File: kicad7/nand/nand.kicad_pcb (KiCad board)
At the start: 2 copper layers, 43.2 x 27.9 mm, 15 parts, among them J1 Conn_01x06_Pin, U1 TL074

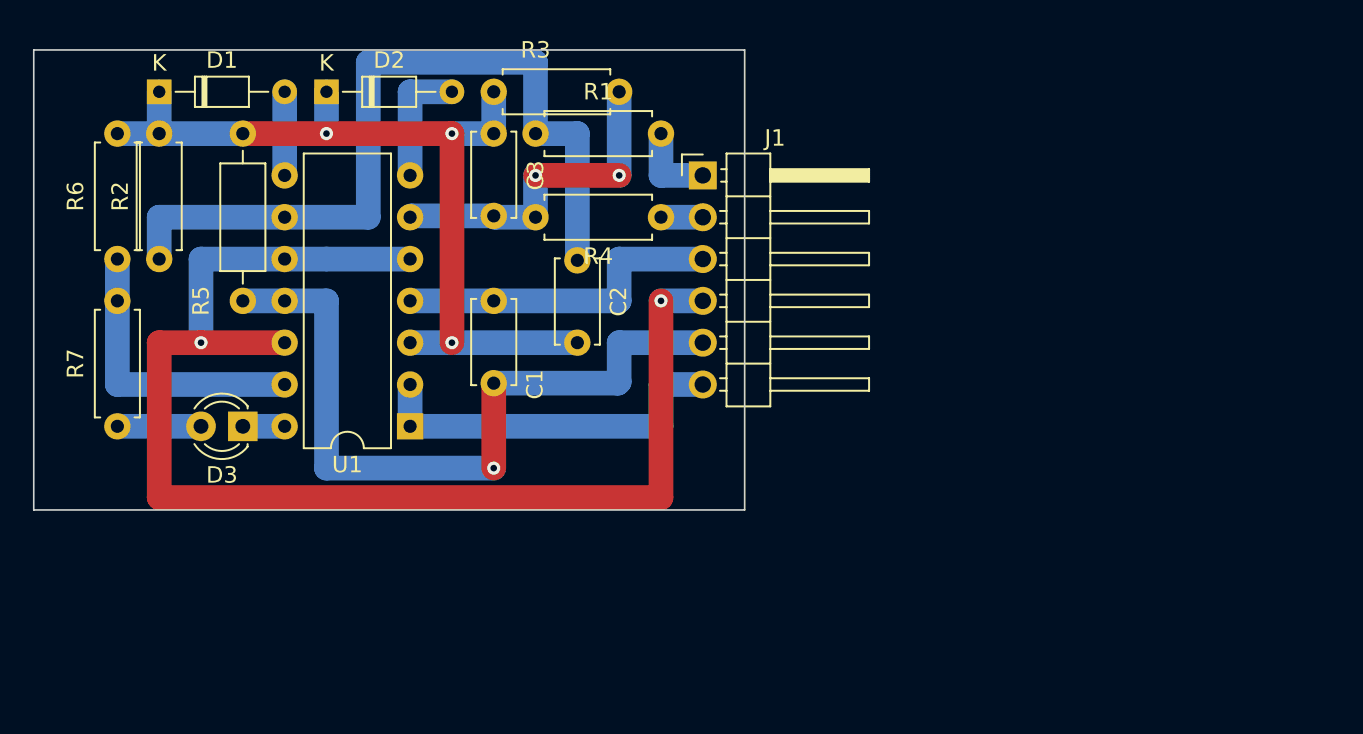
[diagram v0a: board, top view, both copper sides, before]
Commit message: alt nand submodule layout. looking better but a lot of jumpers
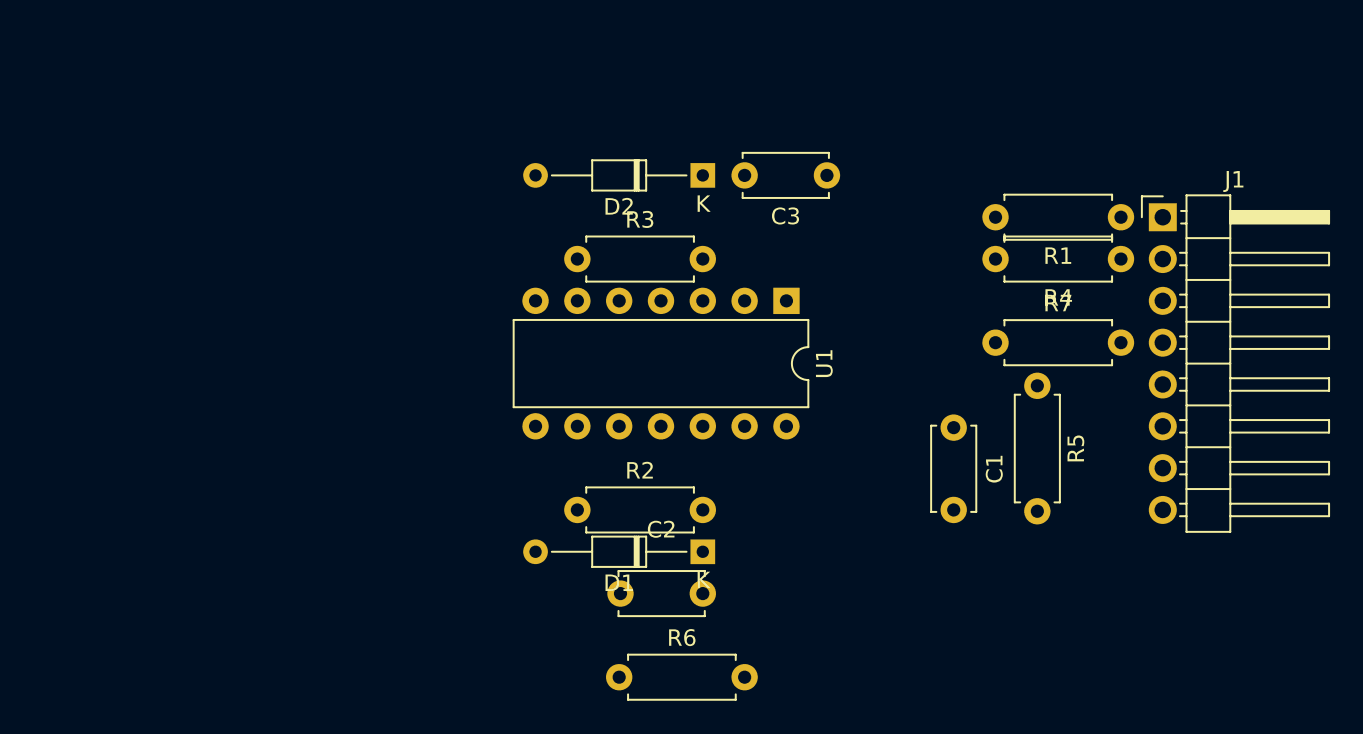
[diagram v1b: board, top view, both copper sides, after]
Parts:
- removed D3: LED_Dual_Bidirectional, LED_THT:LED_D3.0mm
- D1, D2: footprint Diode_THT:D_DO-34_SOD68_P7.62mm_Horizontal -> Diode_THT:D_DO-34_SOD68_P10.16mm_Horizontal
- J1: value Conn_01x06_Pin -> Conn_01x08; footprint Connector_PinHeader_2.54mm:PinHeader_1x06_P2.54mm_Horizontal -> Connector_PinHeader_2.54mm:PinHeader_1x08_P2.54mm_Horizontal
- R5: footprint Resistor_THT:R_Axial_DIN0207_L6.3mm_D2.5mm_P10.16mm_Horizontal -> Resistor_THT:R_Axial_DIN0207_L6.3mm_D2.5mm_P7.62mm_Horizontal
- moved R7 53.4 mm to (149.9, 58.4), turned to 0 degrees
- moved R5 50.6 mm to (152.4, 61.0)
- moved R6 44.9 mm to (127.0, 78.7), turned to 0 degrees
- moved D1 43.3 mm to (132.1, 71.1), turned to 180 degrees
- moved R2 29.6 mm to (124.5, 68.6), turned to 0 degrees
- moved C1 29.0 mm to (147.3, 63.6)
- moved R1 28.4 mm to (157.5, 50.8)
- moved J1 28.1 mm to (160.0, 50.8)
- moved R4 28.1 mm to (157.5, 53.3)
- moved U1 24.1 mm to (137.2, 55.9), turned to -90 degrees
- moved D2 23.4 mm to (132.1, 48.3), turned to 180 degrees
- moved C2 20.4 mm to (127.1, 73.7), turned to 0 degrees
- moved C3 20.4 mm to (139.6, 48.3), turned to 180 degrees
- moved R3 10.5 mm to (124.5, 53.3), turned to 0 degrees
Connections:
- J1 pad 3: +12V -> /single_nand/NAND
- J1 pad 4: GND -> /single_nand/FROM-LED
- J1 pad 5: -12V -> /single_nand/TO-LED
- J1 pad 6: /single_nand/NAND -> +12V
- R7 pad 2: Net-(D3-AK) -> /single_nand/FROM-LED
- U1 pad 14: Net-(D3-KA) -> /single_nand/TO-LED
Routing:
- net GND: track 79.8 -> 0.00 mm, vias 2 -> 0
- net Net-(D1-K): track 53.3 -> 0.00 mm, vias 3 -> 0
- net Net-(U1C--): track 49.3 -> 0.00 mm
- net -12V: track 45.7 -> 0.00 mm, vias 1 -> 0
- net /single_nand/NAND: track 22.9 -> 0.00 mm
- net Net-(U1B--): track 20.4 -> 0.00 mm, vias 2 -> 0
- net +12V: track 20.3 -> 0.00 mm
- net Net-(U1D--): track 17.8 -> 0.00 mm
- net Net-(D2-A): track 7.62 -> 0.00 mm
- net /single_nand/A: track 5.08 -> 0.00 mm
- net Net-(D3-AK): track 5.08 -> 0.00 mm
- net Net-(D1-A): track 5.08 -> 0.00 mm
- net /single_nand/B: track 2.54 -> 0.00 mm
- net Net-(D3-KA): track 2.54 -> 0.00 mm
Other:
- board outline removed
